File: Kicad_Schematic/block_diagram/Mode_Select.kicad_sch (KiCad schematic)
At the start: 3 parts, among them SW1 Push Button

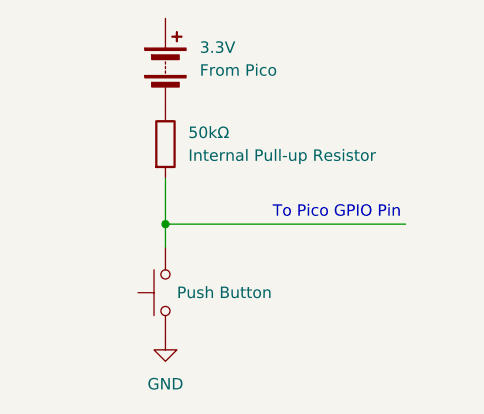
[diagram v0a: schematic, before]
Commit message: Updated mode select block for a 3rd button
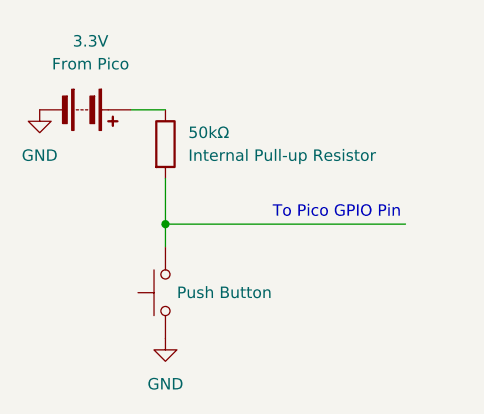
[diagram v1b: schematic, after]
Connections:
- net GND: now also 3.3V.2 (-)
- net at 50kΩ.1: now also 3.3V.1 (+); no longer 3.3V.2 (-)
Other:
- moved on the sheet: 3.3V
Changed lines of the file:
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@@
+		)
+	)
+	(wire
+		(pts
+			(xy 77.47 74.93) (xy 81.28 74.93)
+		)
+		(stroke
+			(width 0)
+			(type default)
 		)
 	)
@@
 	(symbol
 		(lib_id "Device:Battery")
-		(at 81.28 69.85 0)
+		(at 72.39 74.93 270)
 		(unit 1)
 		(exclude_from_sim no)
@@
 		(fields_autoplaced yes)
 		(property "Reference" "3.3V"
-			(at 85.09 68.0084 0)
-			(effects
-				(font
-					(size 1.27 1.27)
-				)
-				(justify left)
+			(at 72.9615 67.31 90)
+			(effects
+				(font
+					(size 1.27 1.27)
+				)
 			)
 		)
 		(property "Value" "From Pico"
-			(at 85.09 70.5484 0)
-			(effects
-				(font
-					(size 1.27 1.27)
-				)
-				(justify left)
-			)
-		)
-		(property "Footprint" ""
-			(at 81.28 68.326 90)
+			(at 72.9615 69.85 90)
+			(effects
+				(font
+					(size 1.27 1.27)
+				)
+			)
+		)
+		(property "Footprint" ""
+			(at 73.914 74.93 90)
 			(effects
 				(font
@@
 		)
 		(property "Datasheet" "~"
-			(at 81.28 68.326 90)
+			(at 73.914 74.93 90)
 			(effects
 				(font
@@
 		)
 		(property "Description" "Multiple-cell battery"
-			(at 81.28 69.85 0)
+			(at 72.39 74.93 0)
 			(effects
 				(font
@@
 					(unit 1)
 				)
+			)
+		)
+	)
+	(symbol
+		(lib_id "power:GND")
+		(at 67.31 74.93 0)
+		(unit 1)
+		(exclude_from_sim no)
+		(in_bom yes)
+		(on_board yes)
+		(dnp no)
+		(fields_autoplaced yes)
+		(property "Reference" "#PWR04"
+			(at 67.31 81.28 0)
+			(effects
+				(font
+					(size 1.27 1.27)
+				)
+				(hide yes)
+			)
+		)
+		(property "Value" "GND"
+			(at 67.31 80.01 0)
+			(effects
+				(font
+					(size 1.27 1.27)
+				)
+			)
+		)
+		(property "Footprint" ""
+			(at 67.31 74.93 0)
+			(effects
+				(font
+					(size 1.27 1.27)
+				)
+				(hide yes)
+			)
+		)
+		(property "Datasheet" ""
+			(at 67.31 74.93 0)
+			(effects
+				(font
+					(size 1.27 1.27)
+				)
+				(hide yes)
+			)
+		)
+		(property "Description" "Power symbol creates a global label with name \"GND\" , ground"
+			(at 67.31 74.93 0)
+			(effects
+				(font
+					(size 1.27 1.27)
+				)
+				(hide yes)
+			)
+		)
+		(pin "1"
+		)
+		(instances
+			(project ""
+				(path "/7a474c3b-855e-4a89-97e9-3d42055b899d/926b30cc-e3b3-4831-947e-f4c697cfd91e"
+					(reference "#PWR04")
+					(unit 1)
+				)

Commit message: edited block diagrams from design rev 2
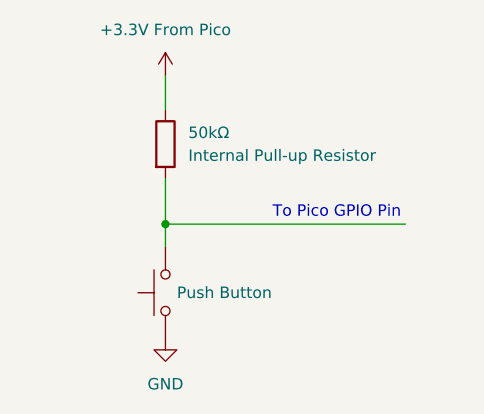
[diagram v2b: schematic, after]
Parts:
- removed 3.3V: From Pico, symbol Device:Battery
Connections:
- net +3.3V From Pico: now reaches 50kΩ.1
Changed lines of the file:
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@@
+	(wire
+		(pts
+			(xy 81.28 71.12) (xy 81.28 74.93)
+		)
+		(stroke
+			(width 0)
+			(type default)
+		)
+	)
 	(wire
 		(pts
@@
 		)
 	)
-	(wire
-		(pts
-			(xy 77.47 74.93) (xy 81.28 74.93)
-		)
-		(stroke
-			(width 0)
-			(type default)
+	(symbol
+		(lib_id "power:+3.3V")
+		(at 81.28 71.12 0)
+		(unit 1)
+		(exclude_from_sim no)
+		(in_bom yes)
+		(on_board yes)
+		(dnp no)
+		(fields_autoplaced yes)
+		(property "Reference" "#PWR06"
+			(at 81.28 74.93 0)
+			(effects
+				(font
+					(size 1.27 1.27)
+				)
+				(hide yes)
+			)
+		)
+		(property "Value" "+3.3V From Pico"
+			(at 81.28 66.04 0)
+			(effects
+				(font
+					(size 1.27 1.27)
+				)
+			)
+		)
+		(property "Footprint" ""
+			(at 81.28 71.12 0)
+			(effects
+				(font
+					(size 1.27 1.27)
+				)
+				(hide yes)
+			)
+		)
+		(property "Datasheet" ""
+			(at 81.28 71.12 0)
+			(effects
+				(font
+					(size 1.27 1.27)
+				)
+				(hide yes)
+			)
+		)
+		(property "Description" "Power symbol creates a global label with name \"+3.3V\""
+			(at 81.28 71.12 0)
+			(effects
+				(font
+					(size 1.27 1.27)
+				)
+				(hide yes)
+			)
+		)
+		(pin "1"
+		)
+		(instances
+			(project ""
+				(path "/7a474c3b-855e-4a89-97e9-3d42055b899d/926b30cc-e3b3-4831-947e-f4c697cfd91e"
+					(reference "#PWR06")
+					(unit 1)
+				)
+			)
 		)
 	)
@@
 					(unit 1)
 				)
-			)
-		)
-	)
-	(symbol
-		(lib_id "Device:Battery")
-		(at 72.39 74.93 270)
-		(unit 1)
-		(exclude_from_sim no)
-		(in_bom yes)
-		(on_board yes)
-		(dnp no)
-		(fields_autoplaced yes)
-		(property "Reference" "3.3V"
-			(at 72.9615 67.31 90)
-			(effects
-				(font
-					(size 1.27 1.27)
-				)
-			)
-		)
-		(property "Value" "From Pico"
-			(at 72.9615 69.85 90)
-			(effects
-				(font
-					(size 1.27 1.27)
-				)
-			)
-		)
-		(property "Footprint" ""
-			(at 73.914 74.93 90)
-			(effects
-				(font
-					(size 1.27 1.27)
-				)
-				(hide yes)
-			)
-		)
-		(property "Datasheet" "~"
-			(at 73.914 74.93 90)
-			(effects
-				(font
-					(size 1.27 1.27)
-				)
-				(hide yes)
-			)
-		)
-		(property "Description" "Multiple-cell battery"
-			(at 72.39 74.93 0)
-			(effects
-				(font
-					(size 1.27 1.27)
-				)
-				(hide yes)
-			)
-		)
-		(pin "2"
-		)
-		(pin "1"
-		)
-		(instances
-			(project ""
-				(path "/7a474c3b-855e-4a89-97e9-3d42055b899d/926b30cc-e3b3-4831-947e-f4c697cfd91e"
-					(reference "3.3V")
-					(unit 1)
-				)
-			)
-		)
-	)
-	(symbol
-		(lib_id "power:GND")
-		(at 67.31 74.93 0)
-		(unit 1)
-		(exclude_from_sim no)
-		(in_bom yes)
-		(on_board yes)
-		(dnp no)
-		(fields_autoplaced yes)
-		(property "Reference" "#PWR04"
-			(at 67.31 81.28 0)
-			(effects
-				(font
-					(size 1.27 1.27)
-				)
-				(hide yes)
-			)
-		)
-		(property "Value" "GND"
-			(at 67.31 80.01 0)
-			(effects
-				(font
-					(size 1.27 1.27)
-				)
-			)
-		)
-		(property "Footprint" ""
-			(at 67.31 74.93 0)
-			(effects
-				(font
-					(size 1.27 1.27)
-				)
-				(hide yes)
-			)
-		)
-		(property "Datasheet" ""
-			(at 67.31 74.93 0)
-			(effects
-				(font
-					(size 1.27 1.27)
-				)
-				(hide yes)
-			)
-		)
-		(property "Description" "Power symbol creates a global label with name \"GND\" , ground"
-			(at 67.31 74.93 0)
-			(effects
-				(font
-					(size 1.27 1.27)
-				)
-				(hide yes)
-			)
-		)
-		(pin "1"
-		)
-		(instances
-			(project ""
-				(path "/7a474c3b-855e-4a89-97e9-3d42055b899d/926b30cc-e3b3-4831-947e-f4c697cfd91e"
-					(reference "#PWR04")
-					(unit 1)
-				)
